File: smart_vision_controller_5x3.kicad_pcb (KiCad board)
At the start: 2 copper layers, 121.3 x 67.3 mm, 36 parts, among them J1 DB9F, J2 DB9M, J3 M12-5_RCPT_F, J4 M12-5_RCPT_F, P1 MINI_FIT_JR_02X03_M_RA, P2 PWR_JACK_2.5x5.5, U1 SN74ABT541BDWR, U2 SN74ABT541BDWR

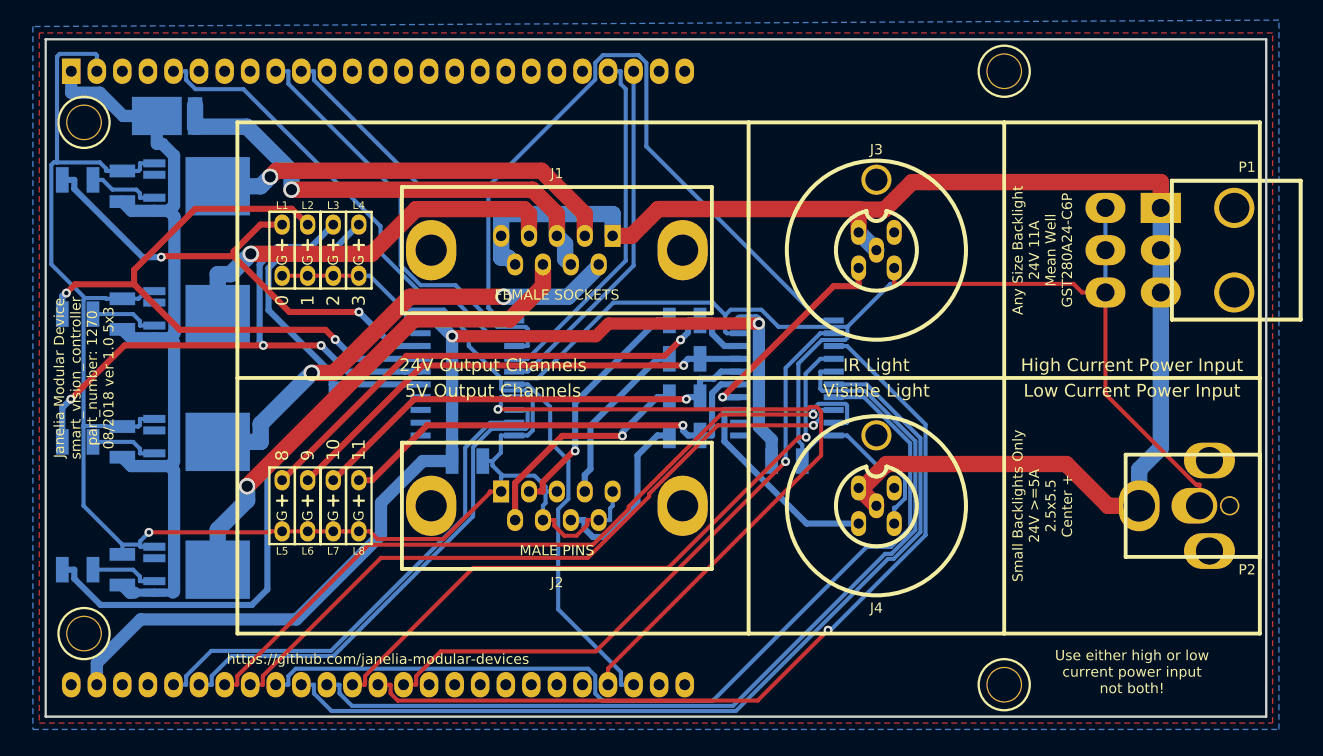
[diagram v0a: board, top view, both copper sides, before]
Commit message: Added 24V led and swapped green led for one in stock.
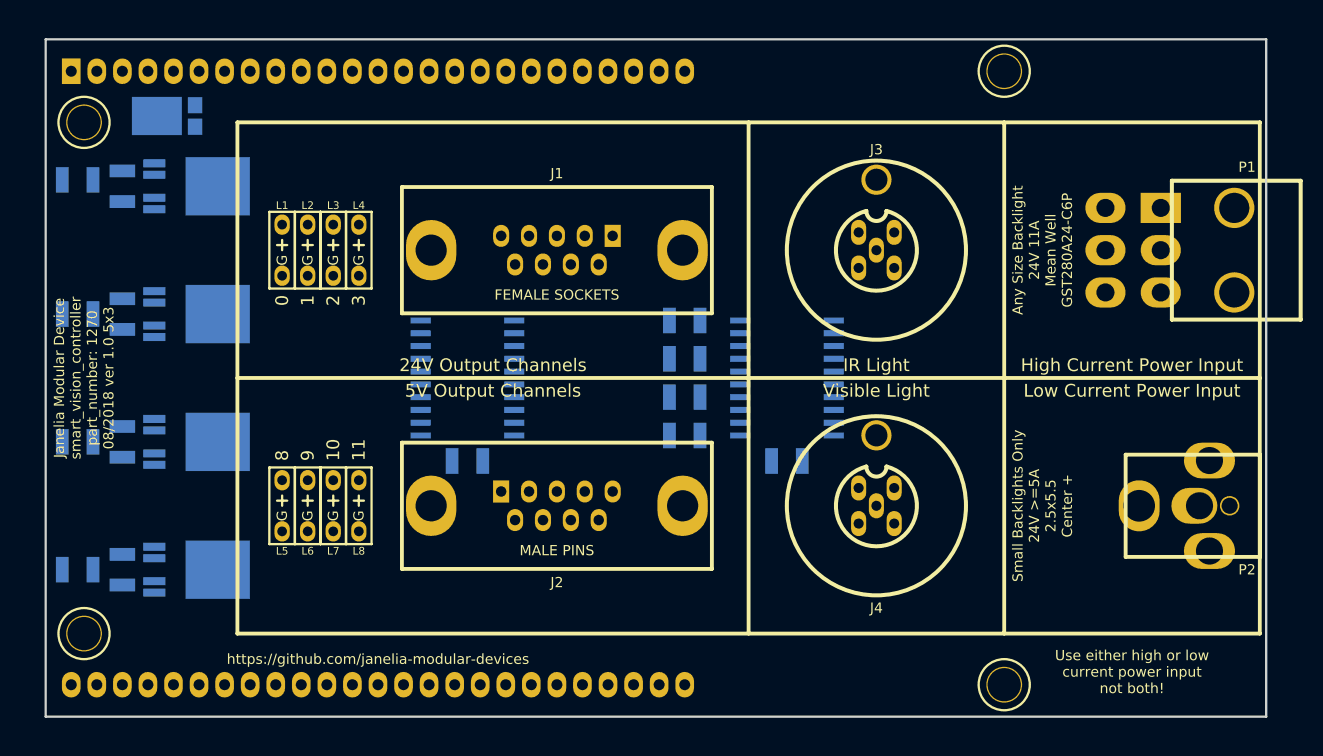
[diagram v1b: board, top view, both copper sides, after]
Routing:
- net GND: track 337.9 -> 0.00 mm, vias 1 -> 0
- net VAA: track 197.3 -> 0.00 mm, vias 1 -> 0
- net VEE: track 111.2 -> 0.00 mm, vias 2 -> 0
- net /~ENABLE: track 95.5 -> 0.00 mm
- net /SIGNAL_13: track 91.6 -> 0.00 mm
- net /SIGNAL_12: track 90.6 -> 0.00 mm
- net /SIGNAL_11: track 90.6 -> 0.00 mm
- net /SIGNAL_9: track 85.7 -> 0.00 mm, vias 1 -> 0
- net VDD: track 82.1 -> 0.00 mm
- net /S_3: track 79.8 -> 0.00 mm
- net /SIGNAL_15: track 77.5 -> 0.00 mm, vias 1 -> 0
- net /SIGNAL_5: track 71.0 -> 0.00 mm, vias 1 -> 0
- net /SIGNAL_14: track 70.5 -> 0.00 mm, vias 1 -> 0
- net /SIGNAL_10: track 65.5 -> 0.00 mm, vias 1 -> 0
- net /SIGNAL_8: track 63.2 -> 0.00 mm, vias 1 -> 0
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- removed copper zone on B.Cu, net GND
- removed copper zone on F.Cu, net VAA

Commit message: Switched back to smaller leds.
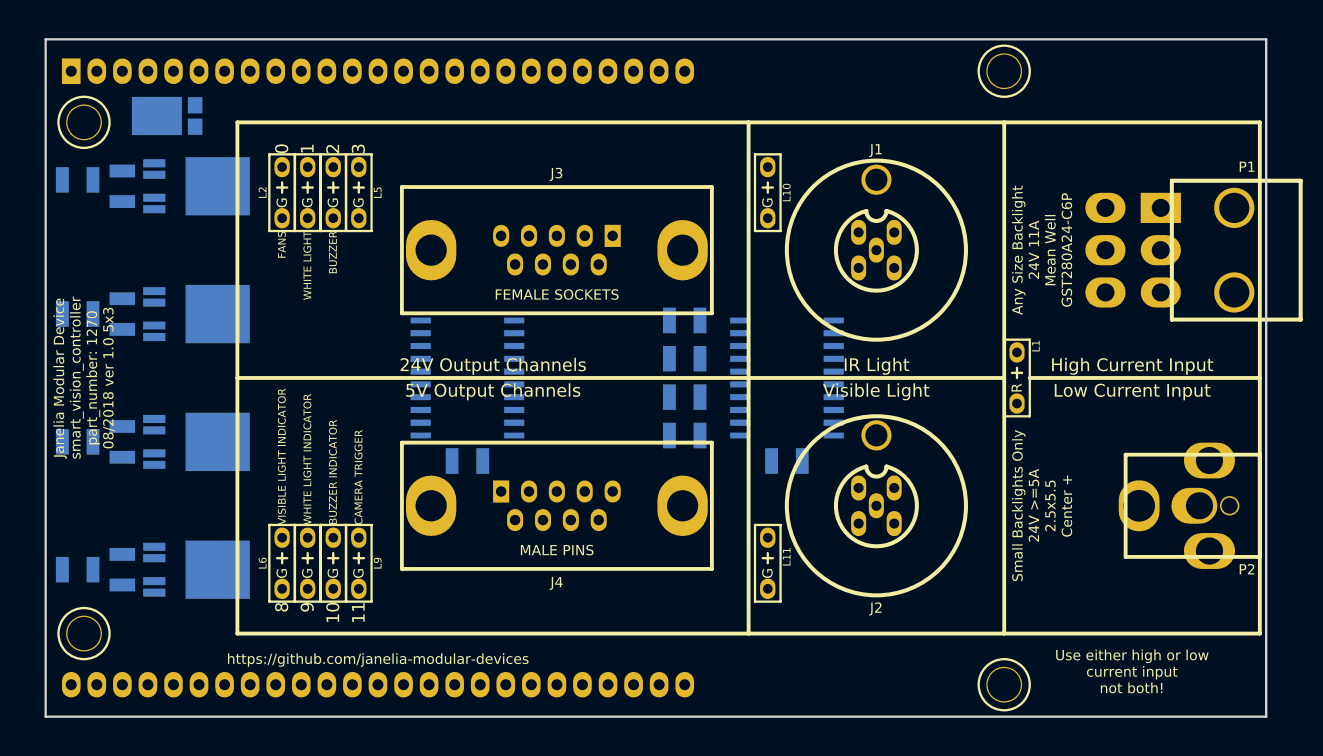
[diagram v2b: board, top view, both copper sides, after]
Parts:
- added L10: LED_5V_GRN, smart_vision_controller_5x3:LED_555-3XXX_G, F.Cu at (141.6, 87.0)
- added L11: LED_5V_GRN, smart_vision_controller_5x3:LED_555-3XXX_G, F.Cu at (141.6, 123.8)
- added L9: LED_5V_GRN, smart_vision_controller_5x3:LED_555-3XXX_G, F.Cu at (101.0, 123.8)
- L1: value LED_5V_GRN -> LED_24V_RED; footprint smart_vision_controller_5x3:LED_555-3XXX_G -> smart_vision_controller_5x3:LED_555-3XXX_R
- moved L1 74.1 mm to (166.4, 105.4)
- moved L5 32.0 mm to (101.0, 87.0)
- moved L6 6.25 mm to (93.3, 123.8)
- moved L8 6.25 mm to (98.4, 123.8)
- moved L7 6.25 mm to (95.9, 123.8)
- moved L2 6.25 mm to (93.3, 87.0)
- moved L4 6.25 mm to (98.4, 87.0)
- moved L3 6.25 mm to (95.9, 87.0)
- renumbered J3 to J1, J4 to J2, J1 to J3, J2 to J4
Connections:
- net /IR renamed /CHANNEL_IR
- net /VISIBLE renamed /CHANNEL_VISIBLE
- L1 pad 1: /S_0 -> VAA
- L2 pad 1: /S_1 -> /S_0
- L3 pad 1: /S_2 -> /S_1
- L4 pad 1: /S_3 -> /S_2
- L5 pad 1: /S_8 -> /S_3
- L6 pad 1: /S_9 -> /S_8
- L7 pad 1: /S_10 -> /S_9
- L8 pad 1: /S_11 -> /S_10
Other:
- board text added: "BUZZER"
- board text added: "BUZZER INDICATOR"
- board text added: "CAMERA TRIGGER"
- board text added: "FANS"
- board text added: "High Current Input"
- board text added: "Low Current Input"
- board text added: "Use either high or low current input not both!"
- board text added: "VISIBLE LIGHT INDICATOR"
- board text added: "WHITE LIGHT"
- board text added: "WHITE LIGHT INDICATOR"
- board text removed: "High Current Power Input"
- board text removed: "Low Current Power Input"
- board text removed: "Use either high or low current power input not both!"

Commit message: Rerouted traces.
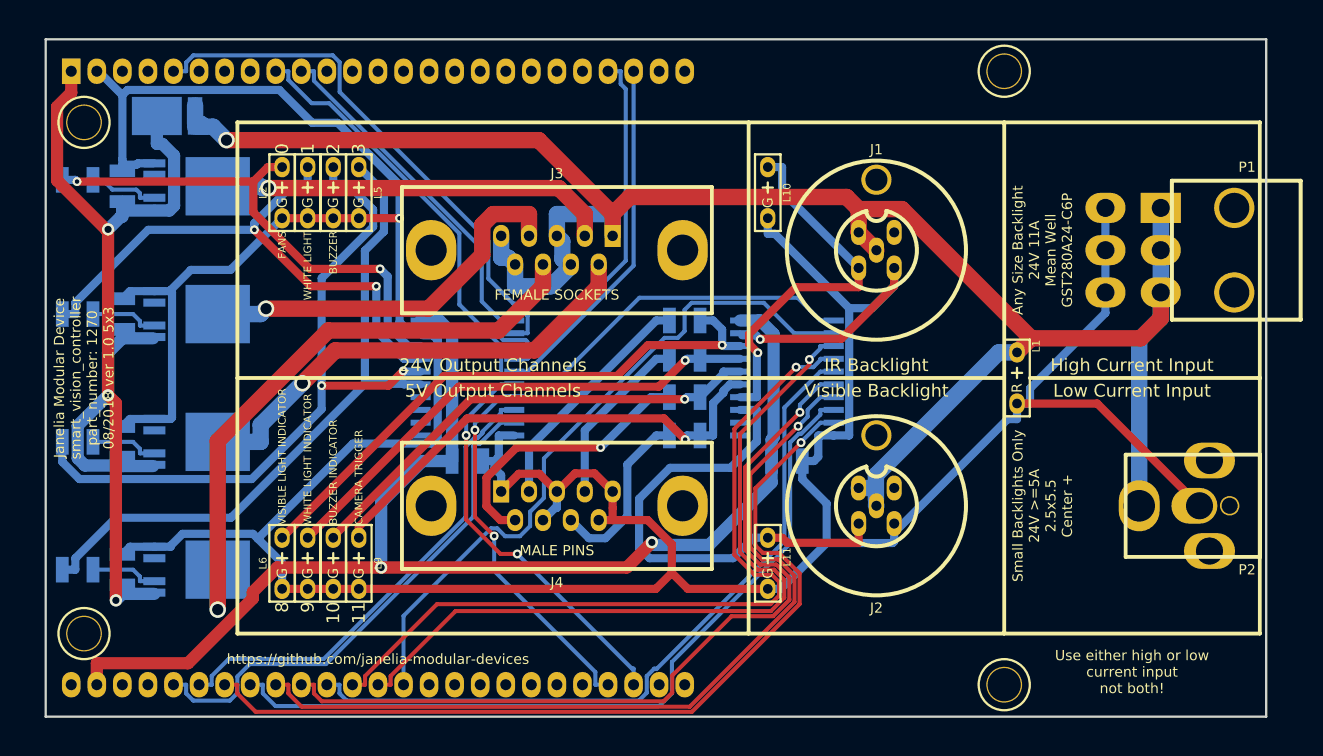
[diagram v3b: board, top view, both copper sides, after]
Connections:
- net /CHANNEL_IR renamed /C_12
- net /CHANNEL_VISIBLE renamed /C_13
- net /SIGNAL_12 renamed /CHANNEL_12
- net /SIGNAL_13 renamed /CHANNEL_13
- net /SIGNAL_14 renamed /CHANNEL_14
- net /SIGNAL_15 renamed /CHANNEL_15
- net /SIGNAL_4 renamed /CHANNEL_4
- net /SIGNAL_5 renamed /CHANNEL_5
- net /SIGNAL_6 renamed /CHANNEL_6
- net /SIGNAL_7 renamed /CHANNEL_7
- net /S_0 renamed /C_0
- net /S_1 renamed /C_1
- net /S_10 renamed /C_10
- net /S_11 renamed /C_11
- net /S_2 renamed /C_2
- net /S_3 renamed /C_3
- net /S_8 renamed /C_8
- net /S_9 renamed /C_9
- net /channel_0/FAULT renamed /output_0/FAULT
- net /channel_1/FAULT renamed /output_1/FAULT
- net /channel_2/FAULT renamed /output_2/FAULT
- net /channel_3/FAULT renamed /output_3/FAULT
- HPS1 pad 6: /CHANNEL_0 -> /FANS
- HPS2 pad 6: /CHANNEL_1 -> /WHITE_LIGHT
- HPS3 pad 6: /CHANNEL_2 -> /BUZZER
- HPS4 pad 6: /CHANNEL_3 -> /OUTPUT_3
- J3 pad 2: /CHANNEL_0 -> /FANS
- J3 pad 4: /CHANNEL_1 -> /WHITE_LIGHT
- J3 pad 6: /CHANNEL_2 -> /BUZZER
- J3 pad 8: /CHANNEL_3 -> /OUTPUT_3
- J4 pad 2: /CHANNEL_8 -> /VISIBLE_LIGHT_INDICATOR
- J4 pad 4: /CHANNEL_9 -> /WHITE_LIGHT_INDICATOR
- J4 pad 6: /CHANNEL_10 -> /BUZZER_INDICATOR
- J4 pad 8: /CHANNEL_11 -> /CAMERA_TRIGGER
- MDB1 pad 14: /SIGNAL_8 -> /CHANNEL_8
- MDB1 pad 15: /SIGNAL_9 -> /CHANNEL_9
- MDB1 pad 16: /SIGNAL_10 -> /CHANNEL_10
- MDB1 pad 17: /SIGNAL_11 -> /CHANNEL_11
- MDB1 pad 2: /SIGNAL_0 -> /CHANNEL_0
- MDB1 pad 29: /SIGNAL_2 -> /CHANNEL_2
- MDB1 pad 30: /SIGNAL_3 -> /CHANNEL_3
- MDB1 pad 6: /SIGNAL_1 -> /CHANNEL_1
- R5 pad 1: /CHANNEL_8 -> /VISIBLE_LIGHT_INDICATOR
- R6 pad 1: /CHANNEL_9 -> /WHITE_LIGHT_INDICATOR
- R7 pad 1: /CHANNEL_10 -> /BUZZER_INDICATOR
- R8 pad 1: /CHANNEL_11 -> /CAMERA_TRIGGER
- U1 pad 2: /SIGNAL_0 -> /CHANNEL_0
- U1 pad 3: /SIGNAL_1 -> /CHANNEL_1
- U1 pad 4: /SIGNAL_2 -> /CHANNEL_2
- U1 pad 5: /SIGNAL_3 -> /CHANNEL_3
- U2 pad 2: /SIGNAL_8 -> /CHANNEL_8
- U2 pad 3: /SIGNAL_9 -> /CHANNEL_9
- U2 pad 4: /SIGNAL_10 -> /CHANNEL_10
- U2 pad 5: /SIGNAL_11 -> /CHANNEL_11
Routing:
- net GND: track 0.00 -> 404.2 mm, vias 0 -> 2
- net VAA: track 0.00 -> 201.5 mm, vias 0 -> 1
- net VEE: track 0.00 -> 127.5 mm, vias 0 -> 2
- net VDD: track 0.00 -> 106.3 mm, vias 0 -> 3
- net /CHANNEL_15: track 0.00 -> 88.0 mm, vias 0 -> 1
- net /CHANNEL_13: track 0.00 -> 84.6 mm, vias 0 -> 1
- net /CHANNEL_12: track 0.00 -> 83.5 mm, vias 0 -> 1
- net /~ENABLE: track 0.00 -> 82.7 mm
- net /CHANNEL_14: track 0.00 -> 79.6 mm
- net /CHANNEL_10: track 0.00 -> 78.8 mm, vias 0 -> 1
- net /CHANNEL_9: track 0.00 -> 76.9 mm, vias 0 -> 1
- net /CHANNEL_11: track 0.00 -> 73.8 mm
- net /C_2: track 0.00 -> 70.5 mm, vias 0 -> 2
- net /CHANNEL_8: track 0.00 -> 68.8 mm
- net /C_3: track 0.00 -> 67.3 mm
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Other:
- net class GND: trace_width 0.4064 -> 0.8128
- net class LEDPOWER: trace_width 0.6096 -> 0.8128
- board text added: "IR Backlight"
- board text added: "Visible Backlight"
- board text removed: "IR Light"
- board text removed: "Visible Light"

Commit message: Added to supplemental bom.
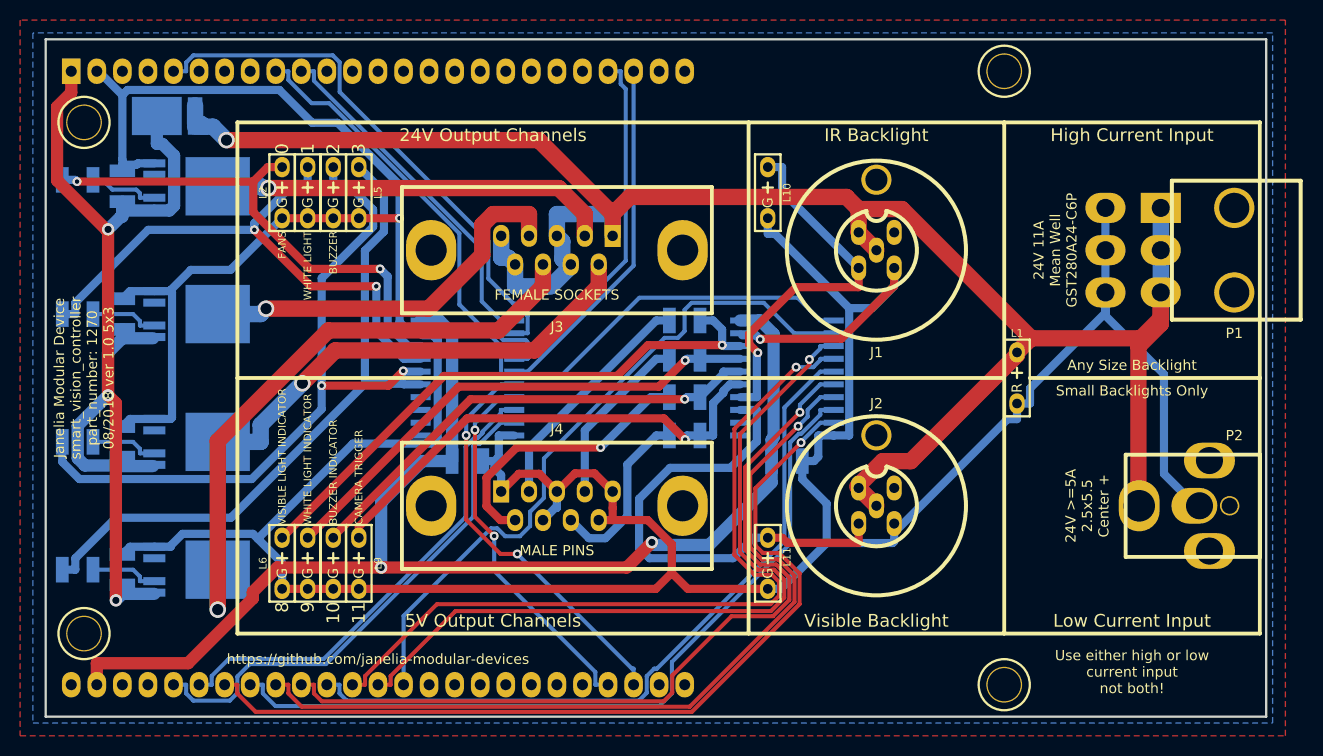
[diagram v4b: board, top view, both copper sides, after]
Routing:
- net GND: track 404.2 -> 406.8 mm
- added copper zone on B.Cu, net GND
- added copper zone on F.Cu, net VAA
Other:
- board text added: "24V 11A Mean Well GST280A24-C6P"
- board text added: "24V >=5A 2.5x5.5 Center +"
- board text added: "Any Size Backlight"
- board text added: "Small Backlights Only"
- board text removed: "Any Size Backlight 24V 11A Mean Well GST280A24-C6P"
- board text removed: "Small Backlights Only 24V >=5A 2.5x5.5 Center +"
